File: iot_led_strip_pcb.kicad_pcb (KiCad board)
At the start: 2 copper layers, 50 x 50 mm, 61 parts, among them J1 I2C Expansion, J2 Conn_01x03_Socket, J3 GT-USB-7010ASV, J4 Barrel_Jack_Switch_Pin3Ring, J5 TC2050-IDC_Cortex-M, J6 Conn_01x03_Socket_Solderwire, J7 PWR_HEADER, J8 UART, Q1 BSS138, SW1 RESET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

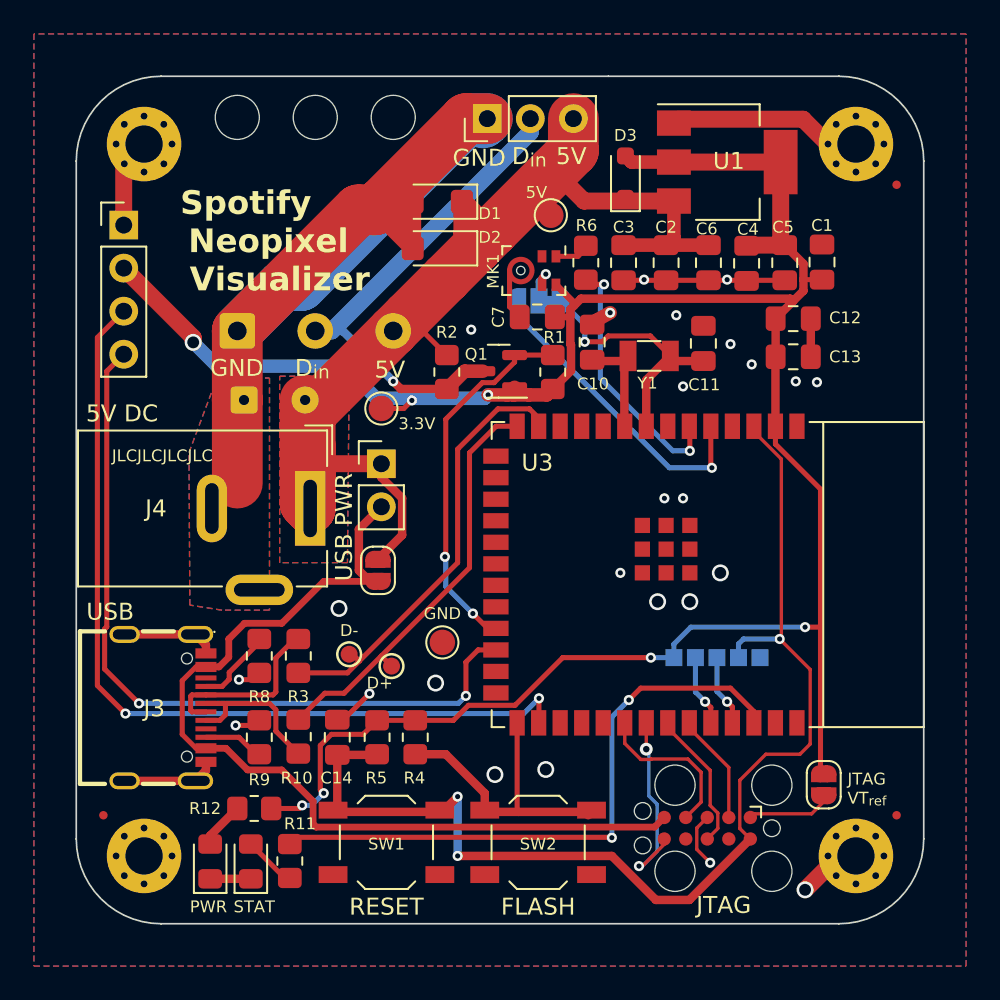
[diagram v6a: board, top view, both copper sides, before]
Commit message: added power led disconnect and cleaned up some traces
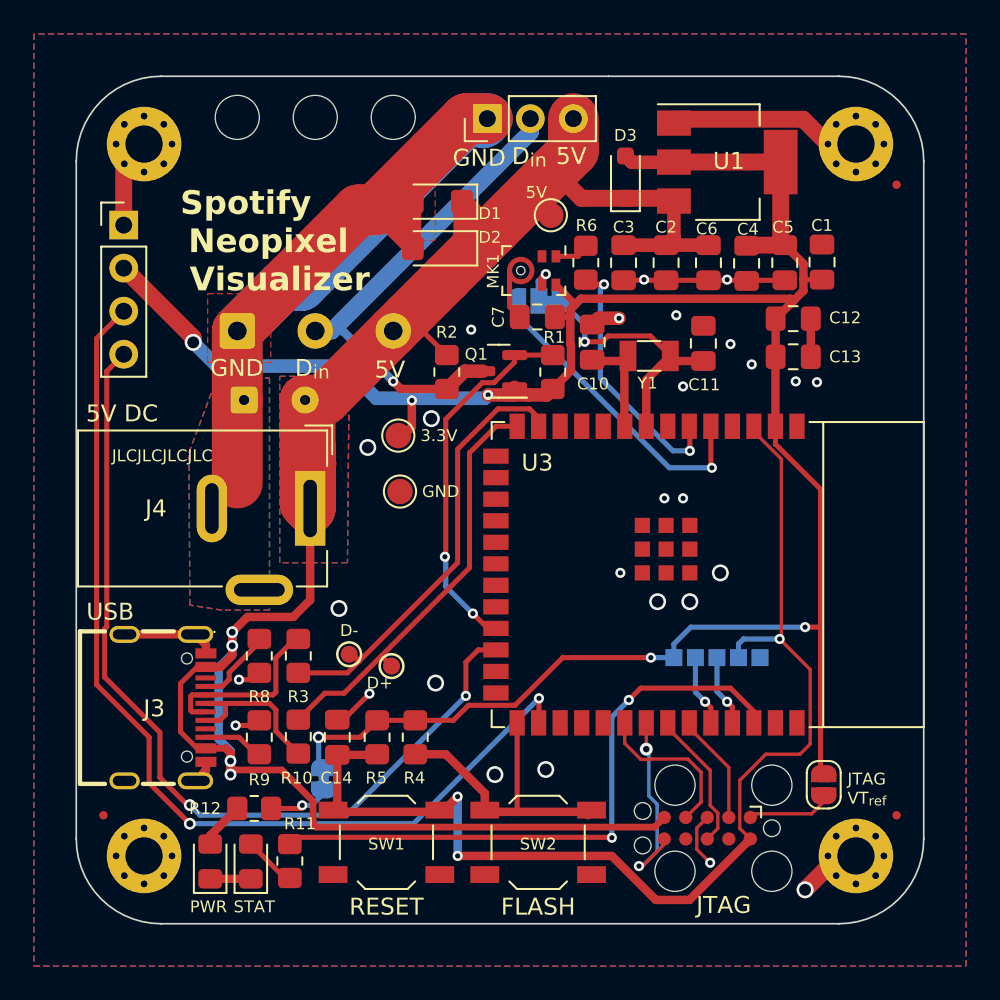
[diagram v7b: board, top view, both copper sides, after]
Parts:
- removed JP3: USB PWR, Jumper:SolderJumper-2_P1.3mm_Open_RoundedPad1.0x1.5mm
- removed JP4: Jumper_2_Bridged, Connector_PinHeader_2.54mm:PinHeader_1x02_P2.54mm_Vertical
- added JP2: PWR_LED_BRIDGE, Jumper:SolderJumper-2_P1.3mm_Bridged_RoundedPad1.0x1.5mm, B.Cu at (124.6, 111.5)
- moved TP3 9.24 mm to (129.1, 94.5)
- moved TP2 1.89 mm to (129.0, 91.2)
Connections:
- J3 pad A4B9: VBUS -> +5V
- J3 pad B4A9: VBUS -> +5V
- J5 pad 5: VBUS -> +5V
- R12 pad 2: +3.3V -> Net-(JP2-A)
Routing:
- net VBUS: track 54.7 -> 0.00 mm
- net +5V: track 75.4 -> 127.8 mm, vias 0 -> 4
- net /SDA: track 45.4 -> 52.7 mm
- net /SCL: track 51.3 -> 58.3 mm
- net +3.3V: track 142.7 -> 138.8 mm, vias 7 -> 6
- net Earth: track 110.1 -> 106.4 mm, vias 25 -> 27
- net Net-(JP2-A): track 0.00 -> 3.47 mm, vias 0 -> 1
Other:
- board text added: "5V DC ONLY"
- board text added: "PWR LED DISABLE"

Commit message: moved i2c SCL to pin on both S2 and S3
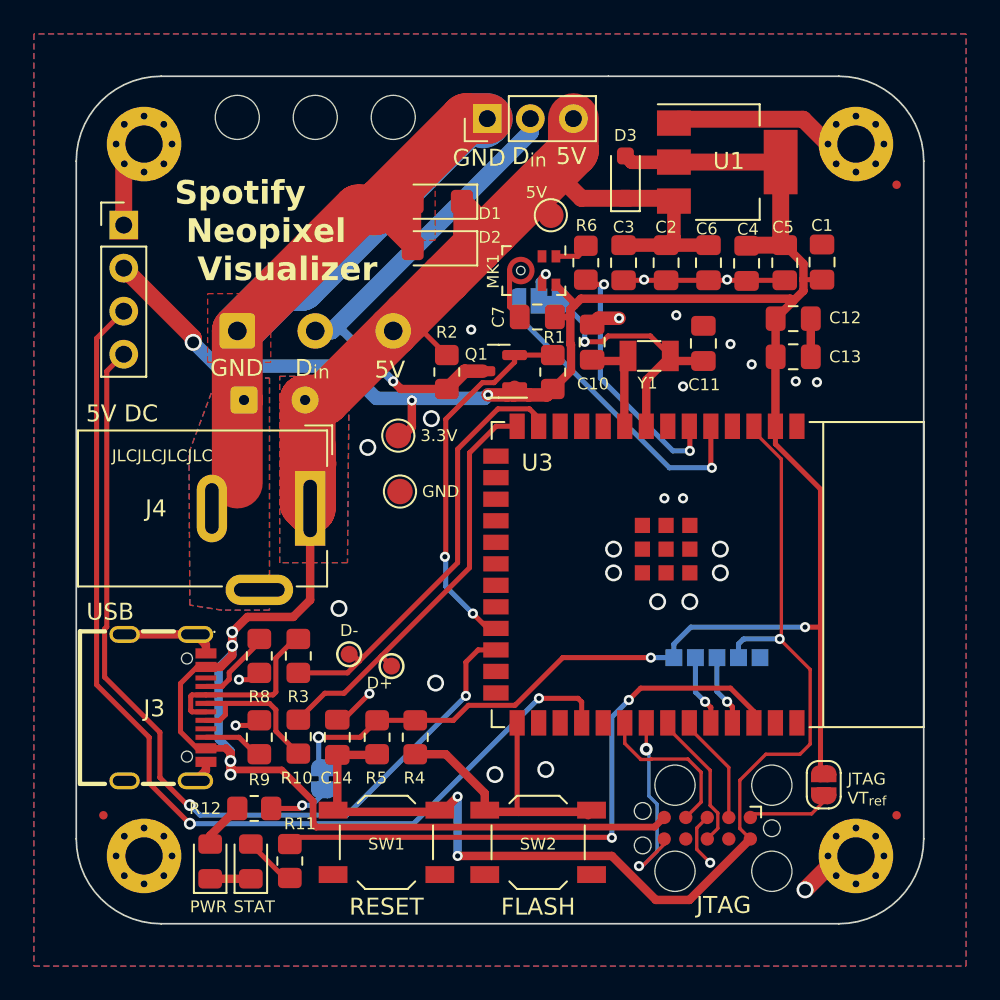
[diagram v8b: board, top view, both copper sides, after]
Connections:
- U3 pad 28: /SCL -> unconnected-(U3-SPIIO6/GPIO35/FSPID-Pad28)
- U3 pad 30: unconnected-(U3-SPIDQS/GPIO37/FSPIQ-Pad30) -> /SCL
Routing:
- net /SCL: track 58.3 -> 60.7 mm
- net Earth: vias 27 -> 29
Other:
- board text added: "v2.2 11-2023"
- board text removed: "PWR LED DISABLE"
- board text removed: "v2.1 10-2023"
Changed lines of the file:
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@@
   (net 48 "unconnected-(U3-GPIO45-Pad26)")
   (net 49 "unconnected-(U3-SPIIO7{slash}GPIO36{slash}FSPICLK-Pad29)")
-  (net 50 "unconnected-(U3-SPIDQS{slash}GPIO37{slash}FSPIQ-Pad30)")
+  (net 50 "unconnected-(U3-SPIIO6{slash}GPIO35{slash}FSPID-Pad28)")
   (net 51 "unconnected-(U3-GPIO38{slash}FSPIWP-Pad31)")
   (net 52 "unconnected-(U3-GPIO1{slash}TOUCH1{slash}ADC1_CH0-Pad39)")
@@
     (descr "Resistor SMD 0805 (2012 Metric), square (rectangular) end terminal, IPC_7351 nominal with elongated pad for handsoldering. (Body size source: IPC-SM-782 page 72, https://www.pcb-3d.com/wordpress/wp-content/uploads/ipc-sm-782a_amendment_1_and_2.pdf), generated with kicad-footprint-generator")
     (tags "resistor handsolder")
-    (property "Description" "100Ω 0805 125mW Chip Resistor")
+    (property "Description" "100Ω 0805 125mW Chip Resistor (R11,R12 1k recommended)")
     (property "LCSC" "C17408")
     (property "Sheetfile" "iot_led_strip_pcb.kicad_sch")
@@
     (descr "Resistor SMD 0805 (2012 Metric), square (rectangular) end terminal, IPC_7351 nominal with elongated pad for handsoldering. (Body size source: IPC-SM-782 page 72, https://www.pcb-3d.com/wordpress/wp-content/uploads/ipc-sm-782a_amendment_1_and_2.pdf), generated with kicad-footprint-generator")
     (tags "resistor handsolder")
-    (property "Description" "100Ω 0805 125mW Chip Resistor")
+    (property "Description" "100Ω 0805 125mW Chip Resistor (R11,R12 1k recommended)")
     (property "LCSC" "C17408")
     (property "Sheetfile" "iot_led_strip_pcb.kicad_sch")
@@
     (descr "Resistor SMD 0805 (2012 Metric), square (rectangular) end terminal, IPC_7351 nominal with elongated pad for handsoldering. (Body size source: IPC-SM-782 page 72, https://www.pcb-3d.com/wordpress/wp-content/uploads/ipc-sm-782a_amendment_1_and_2.pdf), generated with kicad-footprint-generator")
     (tags "resistor handsolder")
-    (property "Description" "100Ω 0805 125mW Chip Resistor")
+    (property "Description" "100Ω 0805 125mW Chip Resistor (R11,R12 1k recommended)")
     (property "LCSC" "C17408")
     (property "Sheetfile" "iot_led_strip_pcb.kicad_sch")
@@
       (net 28 "BOOT") (pinfunction "GPIO0") (pintype "bidirectional"))
     (pad "28" smd rect locked (at 8.75 6.98 90) (size 1.5 0.9) (layers "F.Cu" "F.Paste" "F.Mask")
-      (net 9 "/SCL") (pinfunction "SPIIO6/GPIO35/FSPID") (pintype "bidirectional"))
+      (net 50 "unconnected-(U3-SPIIO6{slash}GPIO35{slash}FSPID-Pad28)") (pinfunction "SPIIO6/GPIO35/FSPID") (pintype "bidirectional+no_connect"))
     (pad "29" smd rect locked (at 8.75 5.71 90) (size 1.5 0.9) (layers "F.Cu" "F.Paste" "F.Mask")
       (net 49 "unconnected-(U3-SPIIO7{slash}GPIO36{slash}FSPICLK-Pad29)") (pinfunction "SPIIO7/GPIO36/FSPICLK") (pintype "bidirectional+no_connect"))
     (pad "30" smd rect locked (at 8.75 4.44 90) (size 1.5 0.9) (layers "F.Cu" "F.Paste" "F.Mask")
-      (net 50 "unconnected-(U3-SPIDQS{slash}GPIO37{slash}FSPIQ-Pad30)") (pinfunction "SPIDQS/GPIO37/FSPIQ") (pintype "bidirectional+no_connect"))
+      (net 9 "/SCL") (pinfunction "SPIDQS/GPIO37/FSPIQ") (pintype "bidirectional"))
     (pad "31" smd rect locked (at 8.75 3.17 90) (size 1.5 0.9) (layers "F.Cu" "F.Paste" "F.Mask")
       (net 51 "unconnected-(U3-GPIO38{slash}FSPIWP-Pad31)") (pinfunction "GPIO38/FSPIWP") (pintype "bidirectional+no_connect"))
@@
     (effects (font (size 0.7 0.7) (thickness 0.11)) (justify left bottom mirror))
   )
-  (gr_text "PWR LED\nDISABLE" (at 121.6 112.9 -90) (layer "B.SilkS")
-    (effects (font (size 0.6 0.6) (thickness 0.08)) (justify left bottom mirror))
-  )
   (gr_text "GND" (at 150.7 104.9 90) (layer "B.SilkS")
     (effects (font (size 0.7 0.7) (thickness 0.11)) (justify left bottom mirror))
@@
     (effects (font (size 0.7 0.7) (thickness 0.11)) (justify left bottom mirror))
   )
-  (gr_text "v2.1 10-2023" (at 146.8 97.1) (layer "B.SilkS")
+  (gr_text "v2.2 11-2023" (at 146.8 97.1) (layer "B.SilkS")
     (effects (font (size 0.7 0.7) (thickness 0.11)) (justify left bottom mirror))
   )
@@
     (effects (font (size 1 1) (thickness 0.15)) (justify left bottom))
   )
-  (gr_text "Spotify \n    Neopixel \n      Visualizer" (at 120 82.8) (layer "F.SilkS" knockout)
-    (effects (font (size 1.4 1.4) (thickness 0.325) bold) (justify bottom))
+  (gr_text "Spotify\n Neopixel\n  Visualizer" (at 115.8 82.2) (layer "F.SilkS" knockout)
+    (effects (font (size 1.4 1.4) (thickness 0.325) bold) (justify left bottom))
   )
   (gr_text "5V" (at 138.3 75.3) (layer "F.SilkS" knockout)
@@
   (via (at 127.3 106.4235) (size 0.6) (drill 0.3) (layers "F.Cu" "B.Cu") (net 1))
   (via (at 144.7 94.9) (size 0.6) (drill 0.3) (layers "F.Cu" "B.Cu") (free) (net 1))
+  (via (at 141.7 99.3) (size 1) (drill 0.7) (layers "F.Cu" "B.Cu") (free) (net 1))
   (via (at 142.025 84.275) (size 0.6) (drill 0.3) (layers "F.Cu" "B.Cu") (net 1))
   (via (at 119.4 108.3) (size 0.6) (drill 0.3) (layers "F.Cu" "B.Cu") (free) (net 1))
   (via (at 148.6 85.8) (size 0.6) (drill 0.3) (layers "F.Cu" "B.Cu") (free) (net 1))
+  (via (at 148 97.9) (size 1) (drill 0.7) (layers "F.Cu" "B.Cu") (free) (net 1))
   (via (at 133.3 84.95) (size 0.6) (drill 0.3) (layers "F.Cu" "B.Cu") (free) (net 1))
   (via (at 137.7 110.9) (size 1) (drill 0.7) (layers "F.Cu" "B.Cu") (free) (net 1))
@@
   (via (at 130.95 90.2) (size 1) (drill 0.7) (layers "F.Cu" "B.Cu") (free) (net 1))
   (via (at 143.5 82) (size 0.6) (drill 0.3) (layers "F.Cu" "B.Cu") (net 1))
-  (via (at 142.1 99.3) (size 0.6) (drill 0.3) (layers "F.Cu" "B.Cu") (free) (net 1))
   (via (at 148.4 82) (size 0.6) (drill 0.3) (layers "F.Cu" "B.Cu") (net 1))
+  (via (at 141.7 97.9) (size 1) (drill 0.7) (layers "F.Cu" "B.Cu") (free) (net 1))
   (via (at 153.7 88.05) (size 0.6) (drill 0.3) (layers "F.Cu" "B.Cu") (free) (net 1))
   (segment (start 119.5 85.025) (end 122.177 82.348) (width 3) (layer "B.Cu") (net 1))
@@
   (segment (start 117.297123 113.593253) (end 116.70387 113) (width 0.3) (layer "B.Cu") (net 8))
   (segment (start 132.987969 106.555364) (end 125.95008 113.593253) (width 0.3) (layer "B.Cu") (net 8))
-  (segment (start 137.3 106.7) (end 137.3 108.13) (width 0.3) (layer "F.Cu") (net 9))
   (segment (start 111.2 105.9) (end 114.3 109) (width 0.3) (layer "F.Cu") (net 9))
+  (segment (start 139.82 106.92) (end 139.82 108.15) (width 0.3) (layer "F.Cu") (net 9))
   (segment (start 111.2 85.46) (end 111.2 105.9) (width 0.3) (layer "F.Cu") (net 9))
+  (segment (start 139.6 106.7) (end 139.82 106.92) (width 0.3) (layer "F.Cu") (net 9))
+  (segment (start 137.3 106.7) (end 139.6 106.7) (width 0.3) (layer "F.Cu") (net 9))
   (segment (start 112.8 83.86) (end 111.2 85.46) (width 0.3) (layer "F.Cu") (net 9))
   (segment (start 114.3 111.7) (end 116.7 114.1) (width 0.3) (layer "F.Cu") (net 9))
